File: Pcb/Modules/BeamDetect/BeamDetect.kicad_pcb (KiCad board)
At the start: 2 copper layers, 50.8 x 20.3 mm, 9 parts, among them J1 JACK_RJ45, U3 TSOP585xx, X1 HOLE, X2 HOLE, X3 HOLE, X4 HOLE

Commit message: Update pcbs.
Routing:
- net +3V3: track 34.2 -> 43.9 mm
- net Net-(J1-Pad2): track 45.1 -> 46.0 mm, vias 1 -> 0
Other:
- board text added: "Beam Detect Module 2017-12-02"
- board text removed: "Beam Module 2017-12-02"
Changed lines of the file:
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@@
     (thickness 1.6)
     (drawings 13)
-    (tracks 24)
+    (tracks 25)
     (zones 0)
     (modules 9)
@@
   )
   (setup
-    (last_trace_width 0.254)
+    (last_trace_width 0.762)
     (user_trace_width 0.254)
     (user_trace_width 0.508)
@@
   (gr_line (start 35.5854 41.91) (end 35.5854 49.53) (angle 90) (layer Edge.Cuts) (width 0.15))
   (gr_line (start 86.3854 41.91) (end 86.3854 49.53) (angle 90) (layer Edge.Cuts) (width 0.15))
-  (gr_text "Beam Module\n2017-12-02" (at 54.61 38.1) (layer F.SilkS)
-    (effects (font (size 1.27 1.27) (thickness 0.254)) (justify left))
+  (gr_text "Beam Detect Module\n2017-12-02" (at 50.292 45.466) (layer F.SilkS)
+    (effects (font (size 1.016 1.016) (thickness 0.2032)) (justify left))
   )
   (gr_line (start 80.0354 55.88) (end 41.9354 55.88) (angle 90) (layer Edge.Cuts) (width 0.15))
@@
   (segment (start 82.042 47.498) (end 82.042 45.2) (width 0.762) (layer F.Cu) (net 1))
   (segment (start 80.8152 48.7248) (end 81.788 47.752) (width 0.762) (layer F.Cu) (net 1))
+  (segment (start 42.032 48.25) (end 71.872 48.25) (width 0.762) (layer F.Cu) (net 2))
+  (segment (start 83.566 48.26) (end 84.836 48.26) (width 0.762) (layer F.Cu) (net 2))
+  (segment (start 80.01 51.816) (end 83.566 48.26) (width 0.762) (layer F.Cu) (net 2))
+  (segment (start 75.438 51.816) (end 80.01 51.816) (width 0.762) (layer F.Cu) (net 2))
+  (segment (start 71.872 48.25) (end 75.438 51.816) (width 0.762) (layer F.Cu) (net 2))
   (segment (start 84.836 48.26) (end 84.582 48.26) (width 0.508) (layer F.Cu) (net 2))
-  (segment (start 84.582 48.26) (end 81.788 51.054) (width 0.508) (layer F.Cu) (net 2))
-  (segment (start 81.788 51.054) (end 75.692 51.054) (width 0.508) (layer F.Cu) (net 2))
-  (segment (start 75.692 51.054) (end 72.898 48.26) (width 0.508) (layer F.Cu) (net 2))
-  (segment (start 72.898 48.26) (end 52.07 48.26) (width 0.508) (layer F.Cu) (net 2))
-  (via (at 52.07 48.26) (size 1.016) (drill 0.508) (layers F.Cu B.Cu) (net 2))
-  (segment (start 52.07 48.26) (end 52.06 48.25) (width 0.508) (layer B.Cu) (net 2))
-  (segment (start 52.06 48.25) (end 42.032 48.25) (width 0.508) (layer B.Cu) (net 2))
+  (segment (start 40.252 49.28) (end 40.136 49.28) (width 0.762) (layer F.Cu) (net 3))
+  (segment (start 40.136 49.28) (end 37.846 46.99) (width 0.762) (layer F.Cu) (net 3))
+  (segment (start 46.99 43.942) (end 71.386 43.942) (width 0.762) (layer F.Cu) (net 3))
+  (segment (start 43.434 40.386) (end 46.99 43.942) (width 0.762) (layer F.Cu) (net 3))
+  (segment (start 40.386 40.386) (end 43.434 40.386) (width 0.762) (layer F.Cu) (net 3))
+  (segment (start 37.846 42.926) (end 40.386 40.386) (width 0.762) (layer F.Cu) (net 3))
+  (segment (start 37.846 46.99) (end 37.846 42.926) (width 0.762) (layer F.Cu) (net 3))
   (segment (start 40.252 49.28) (end 40.644 49.28) (width 0.762) (layer F.Cu) (net 3))
-  (segment (start 40.644 49.28) (end 41.656 50.292) (width 0.762) (layer F.Cu) (net 3))
-  (segment (start 41.656 50.292) (end 47.752 50.292) (width 0.762) (layer F.Cu) (net 3))
-  (segment (start 47.752 50.292) (end 54.102 43.942) (width 0.762) (layer F.Cu) (net 3))
-  (segment (start 54.102 43.942) (end 71.386 43.942) (width 0.762) (layer F.Cu) (net 3))
   (segment (start 82.042 43.7) (end 84.316 43.7) (width 0.762) (layer F.Cu) (net 4))
   (segment (start 84.316 43.7) (end 84.836 43.18) (width 0.762) (layer F.Cu) (net 4))

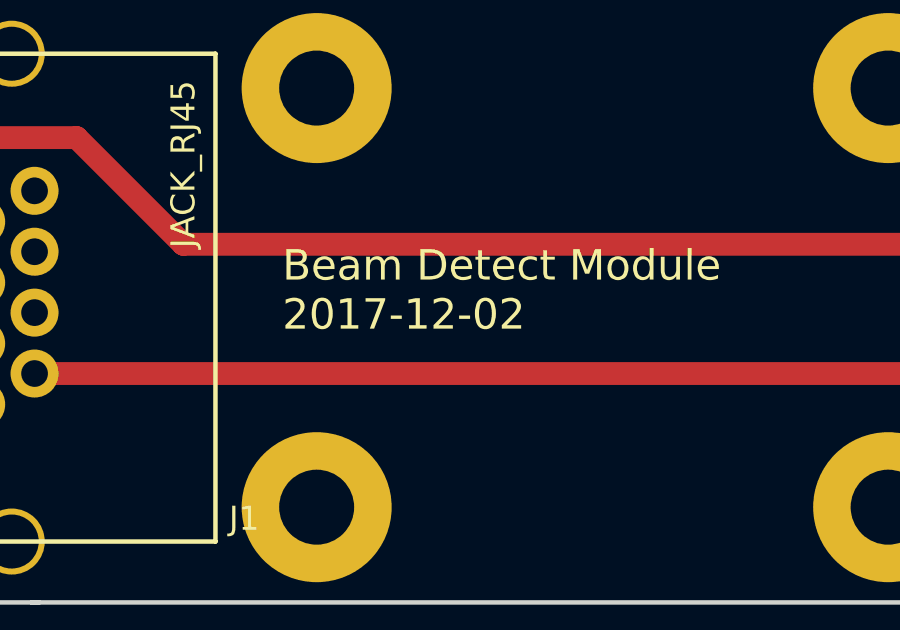
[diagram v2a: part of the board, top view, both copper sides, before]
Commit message: Update CA6 PCB.  Also update versions of all the module pcbs to match.
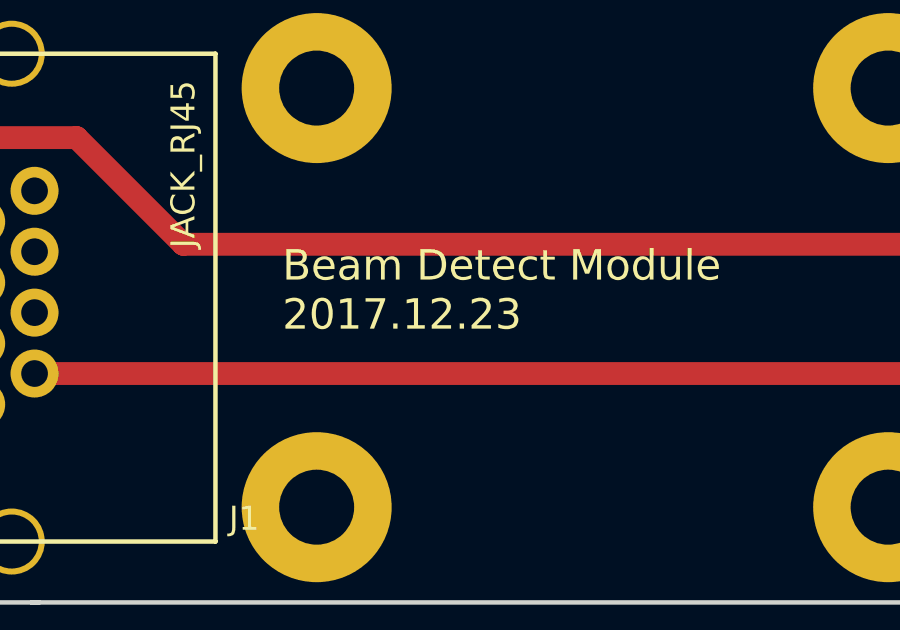
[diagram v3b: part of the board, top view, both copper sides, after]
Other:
- board text added: "Beam Detect Module 2017.12.23"
- board text removed: "Beam Detect Module 2017-12-02"
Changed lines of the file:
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@@
     (links 10)
     (no_connects 0)
-    (area 35.510399 35.484999 86.460401 55.955001)
+    (area 31.983069 34.206 89.500001 57.334)
     (thickness 1.6)
     (drawings 13)
@@
   (gr_line (start 35.5854 41.91) (end 35.5854 49.53) (angle 90) (layer Edge.Cuts) (width 0.15))
   (gr_line (start 86.3854 41.91) (end 86.3854 49.53) (angle 90) (layer Edge.Cuts) (width 0.15))
-  (gr_text "Beam Detect Module\n2017-12-02" (at 50.292 45.466) (layer F.SilkS)
+  (gr_text "Beam Detect Module\n2017.12.23" (at 50.292 45.466) (layer F.SilkS)
     (effects (font (size 1.016 1.016) (thickness 0.2032)) (justify left))
   )
